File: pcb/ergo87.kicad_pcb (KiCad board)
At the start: 2 copper layers, 322.7 x 132.7 mm, 175 parts, among them U1 ItsyBitsy

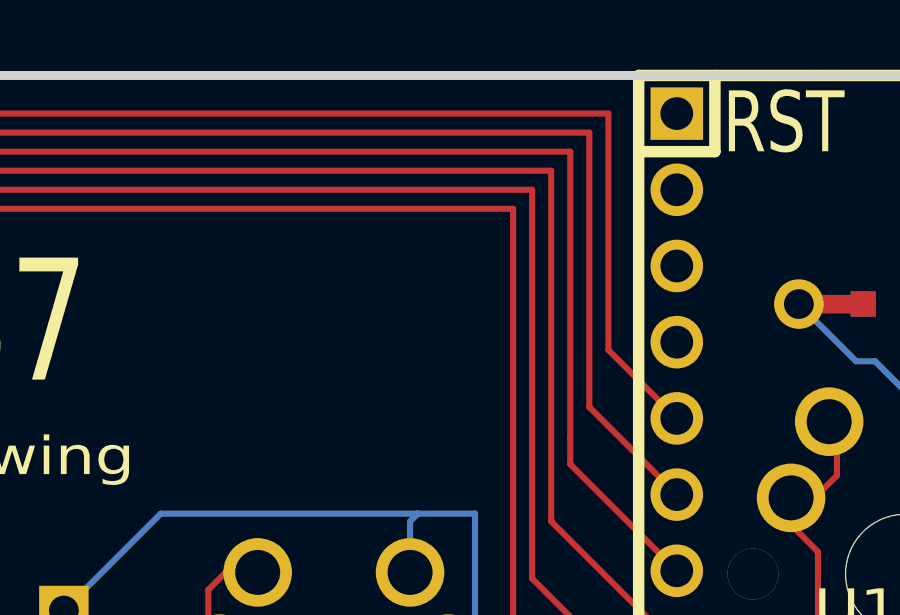
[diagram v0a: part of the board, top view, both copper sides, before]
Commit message: Add reset button footprint
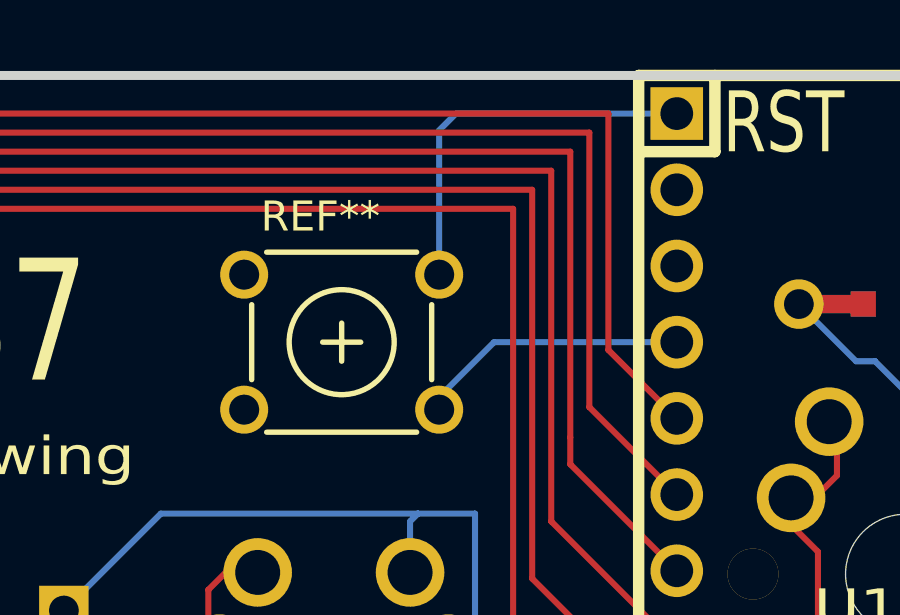
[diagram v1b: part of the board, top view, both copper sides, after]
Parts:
- added REF**: VAL**, B3F-10XX, F.Cu at (156.2, 26.7)
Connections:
- U1 pad 1: (no net) -> N-RST
- U1 pad 4: (no net) -> N-GND
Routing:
- net N-RST: track 0.00 -> 13.0 mm
- net N-GND: track 0.00 -> 9.10 mm
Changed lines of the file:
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@@
 (kicad_pcb (version 4) (host pcbnew 4.0.7)
   (general
-    (links 435)
+    (links 437)
     (no_connects 0)
     (area 13.498331 17.335499 336.501679 150.650001)
     (thickness 1.6002)
     (drawings 11)
-    (tracks 1890)
+    (tracks 1896)
     (zones 0)
-    (modules 175)
-    (nets 109)
+    (modules 176)
+    (nets 111)
   )
   (page User 370.002 189.992)
@@
   (net 107 N-diode-5-13)
   (net 108 N-diode-5-14)
+  (net 109 N-RST)
+  (net 110 N-GND)
   (net_class Default "This is the default net class."
     (clearance 0.254)
@@
     (uvia_dia 0.508)
     (uvia_drill 0.127)
+    (add_net N-GND)
+    (add_net N-RST)
     (add_net N-col-0)
     (add_net N-col-1)
@@
     (fp_line (start -17.78 6.35) (end -15.24 6.35) (layer F.SilkS) (width 0.381))
     (fp_line (start -15.24 6.35) (end -15.24 8.89) (layer F.SilkS) (width 0.381))
-    (pad 1 thru_hole rect (at -16.51 7.62) (size 1.7526 1.7526) (drill 1.0922) (layers *.Cu *.SilkS *.Mask))
+    (pad 1 thru_hole rect (at -16.51 7.62) (size 1.7526 1.7526) (drill 1.0922) (layers *.Cu *.SilkS *.Mask)
+      (net 109 N-RST))
     (pad 2 thru_hole circle (at -13.97 7.62) (size 1.7526 1.7526) (drill 1.0922) (layers *.Cu *.SilkS *.Mask))
     (pad 3 thru_hole circle (at -11.43 7.62) (size 1.7526 1.7526) (drill 1.0922) (layers *.Cu *.SilkS *.Mask))
-    (pad 4 thru_hole circle (at -8.89 7.62) (size 1.7526 1.7526) (drill 1.0922) (layers *.Cu *.SilkS *.Mask))
+    (pad 4 thru_hole circle (at -8.89 7.62) (size 1.7526 1.7526) (drill 1.0922) (layers *.Cu *.SilkS *.Mask)
+      (net 110 N-GND))
     (pad 5 thru_hole circle (at -6.35 7.62) (size 1.7526 1.7526) (drill 1.0922) (layers *.Cu *.SilkS *.Mask)
       (net 7 N-col-0))
@@
     (pad 99 smd rect (at 1.6637 0 10) (size 0.8382 0.8382) (layers Back B.Paste B.Mask))
   )
+  (module B3F-10XX (layer Front)
+    (at 156.21 26.67)
+    (descr "Tactile switch - SPST - 6mm")
+    (tags "tactile switch")
+    (fp_text reference REF** (at -2.7 -3.6) (layer F.SilkS)
+      (effects (font (size 1 1) (thickness 0.18)) (justify left bottom))
+    )
+    (fp_text value VAL** (at 0 4.3) (layer F.SilkS) hide
+      (effects (font (size 1 1) (thickness 0.15)))
+    )
+    (fp_line (start -3.5 -3.5) (end 3.5 -3.5) (layer F.CrtYd) (width 0.05))
+    (fp_line (start 3.5 -3.5) (end 3.5 3.5) (layer F.CrtYd) (width 0.05))
+    (fp_line (start 3.5 3.5) (end -3.5 3.5) (layer F.CrtYd) (width 0.05))
+    (fp_line (start -3.5 3.5) (end -3.5 -3.5) (layer F.CrtYd) (width 0.05))
+    (fp_line (start -3 1.25) (end -3 -1.25) (layer F.SilkS) (width 0.18))
+    (fp_line (start -2.5 3) (end 2.5 3) (layer F.SilkS) (width 0.18))
+    (fp_line (start -2.5 -3) (end 2.5 -3) (layer F.SilkS) (width 0.18))
+    (fp_line (start 3 1.25) (end 3 -1.25) (layer F.SilkS) (width 0.18))
+    (fp_circle (center 0 0) (end 1.75 0) (layer F.SilkS) (width 0.18))
+    (fp_line (start -0.635 0) (end 0.635 0) (layer F.SilkS) (width 0.18))
+    (fp_line (start 0 -0.635) (end 0 0.635) (layer F.SilkS) (width 0.18))
+    (pad 1 thru_hole circle (at -3.25 2.25) (size 1.6 1.6) (drill 1) (layers *.Cu *.Mask))
+    (pad 1 thru_hole circle (at 3.25 2.25) (size 1.6 1.6) (drill 1) (layers *.Cu *.Mask)
+      (net 110 N-GND))
+    (pad 2 thru_hole circle (at 3.25 -2.25) (size 1.6 1.6) (drill 1) (layers *.Cu *.Mask)
+      (net 109 N-RST))
+    (pad 2 thru_hole circle (at -3.25 -2.25) (size 1.6 1.6) (drill 1) (layers *.Cu *.Mask))
+  )
   (gr_text "By: Paul Ewing" (at 141.605 30.48) (layer F.SilkS)
     (effects (font (size 1.27 1.524) (thickness 0.3048)))
@@
   (segment (start 318.3243 115.687382) (end 318.3243 114.7457) (width 0.2032) (layer Back) (net 108))
   (segment (start 318.3243 114.7457) (end 320.675 112.395) (width 0.2032) (layer Back) (net 108))
+  (segment (start 159.46 24.42) (end 159.46 19.61) (width 0.2032) (layer Back) (net 109) (status 400000))
+  (segment (start 160.02 19.05) (end 167.38 19.05) (width 0.2032) (layer Back) (net 109) (status 800000))
+  (segment (start 159.46 19.61) (end 160.02 19.05) (width 0.2032) (layer Back) (net 109))
+  (segment (start 159.46 28.92) (end 159.46 28.5) (width 0.2032) (layer Back) (net 110) (status C00000))
+  (segment (start 159.46 28.5) (end 161.29 26.67) (width 0.2032) (layer Back) (net 110) (status 400000))
+  (segment (start 161.29 26.67) (end 167.38 26.67) (width 0.2032) (layer Back) (net 110) (status 800000))
 )

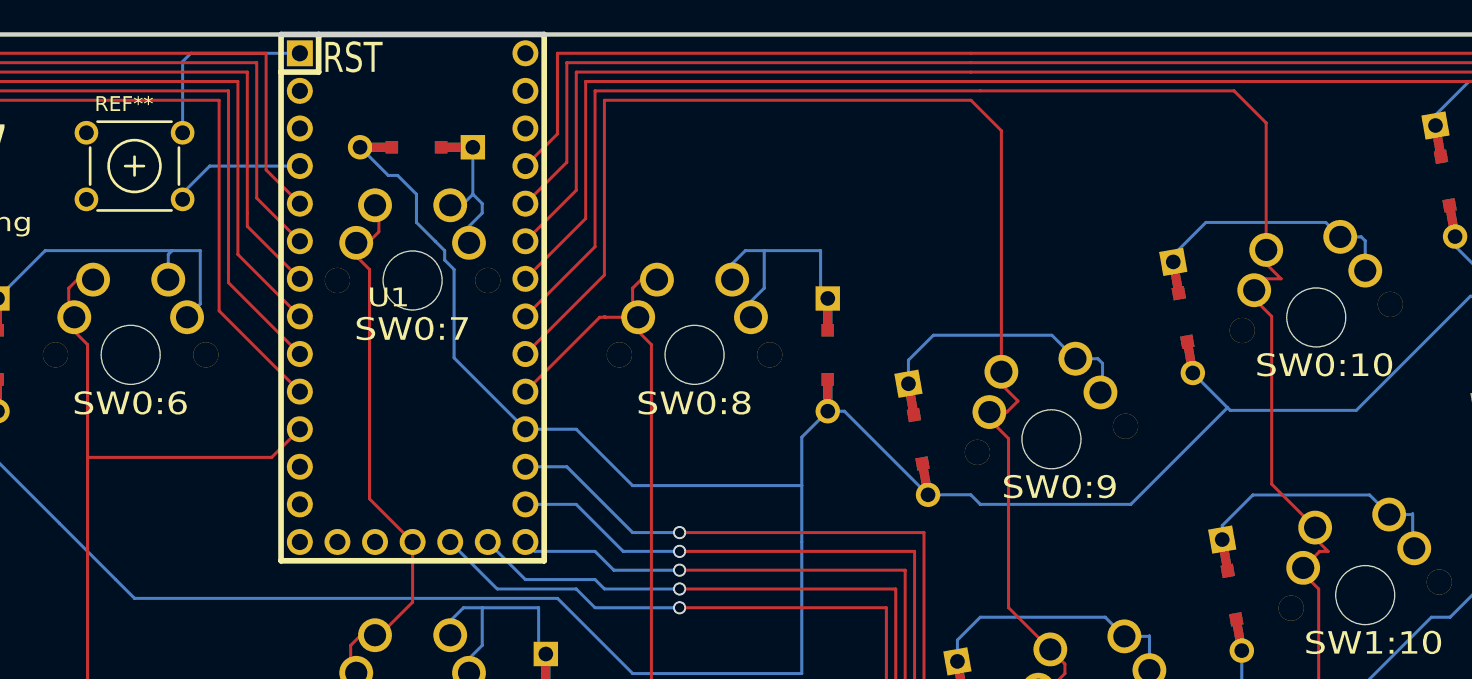
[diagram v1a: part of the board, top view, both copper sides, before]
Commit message: Start working on RGB underglow support
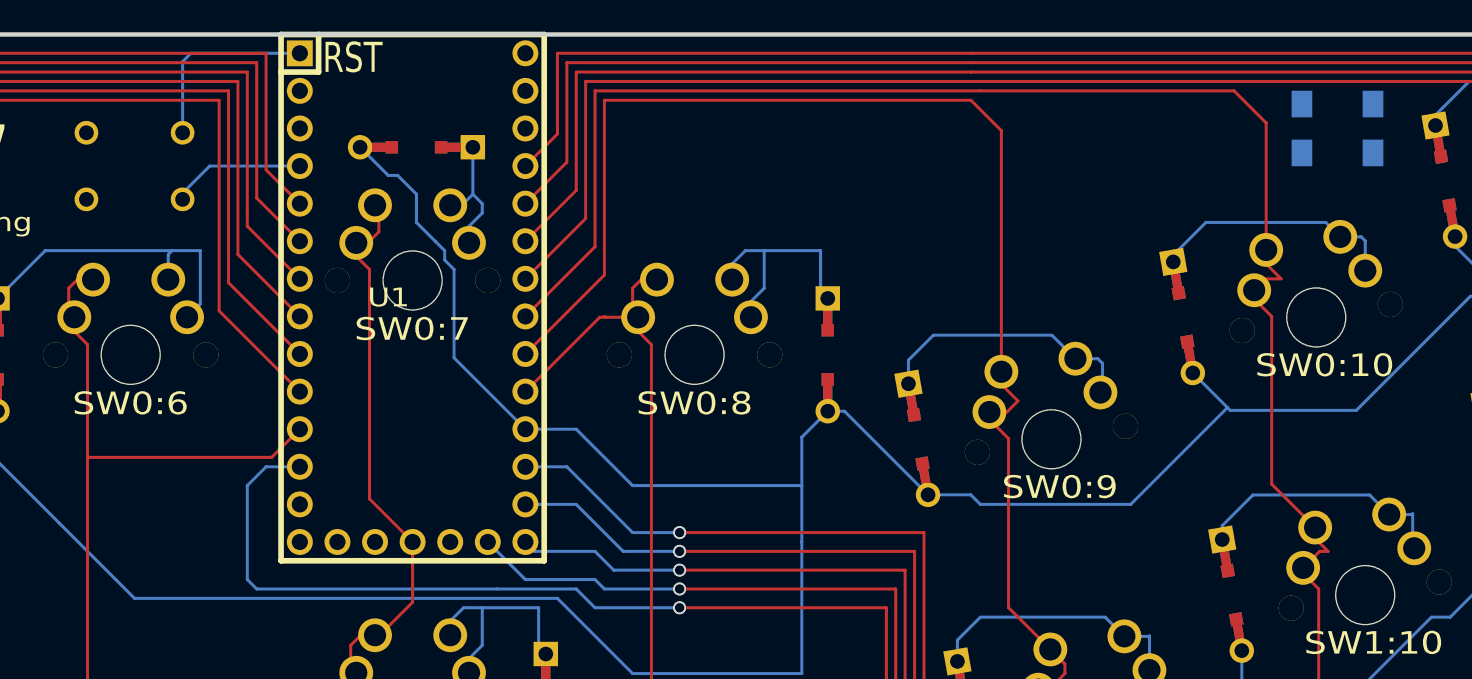
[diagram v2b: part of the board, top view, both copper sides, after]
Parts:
- removed REF**: VAL**, B3F-10XX
- added B1: VAL**, B3F-10XX, B.Cu at (156.2, 26.7)
- added LED?: VAL**, WS2812B, B.Cu at (237.5, 24.1)
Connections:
- U1 pad 12: (no net) -> N-row-5
- U1 pad 17: N-col-7 -> (no net)
- U1 pad 18: N-row-5 -> (no net)
- U1 pad 4: N-GND -> N-GND-0
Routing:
- net N-row-5: track 484.9 -> 507.6 mm
- net N-GND-0: track 0.00 -> 9.10 mm
- net N-GND: track 9.10 -> 0.00 mm

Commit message: Finish the rev2 features
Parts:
- removed LED?: VAL**, WS2812B
- added RGB0: VAL**, WS2812B, B.Cu at (236.9, 22.2)
- added RGB1: VAL**, WS2812B, B.Cu at (318.8, 50.8)
- added RGB10: VAL**, WS2812B, B.Cu at (31.2, 50.8)
- added RGB11: VAL**, WS2812B, B.Cu at (113.1, 22.2)
- added RGB2: VAL**, WS2812B, B.Cu at (328.9, 106.7)
- added RGB3: VAL**, WS2812B, B.Cu at (293.4, 130.2)
- added RGB4: VAL**, WS2812B, B.Cu at (250.8, 139.1)
- added RGB5: VAL**, WS2812B, B.Cu at (197.5, 146.1)
- added RGB6: VAL**, WS2812B, B.Cu at (152.5, 146.1)
- added RGB7: VAL**, WS2812B, B.Cu at (99.2, 139.1)
- added RGB8: VAL**, WS2812B, B.Cu at (56.6, 130.2)
- added RGB9: VAL**, WS2812B, B.Cu at (21.1, 106.7)
- moved B1 73.8 mm to (175.0, 98.0)
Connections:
- U1 pad 17: (no net) -> N-col-7
- U1 pad 18: (no net) -> N-RGB-D0
- U1 pad 2: (no net) -> N-5V-0
- U1 pad 32: (no net) -> N-GND-1
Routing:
- net N-GND-1: track 0.00 -> 931.7 mm, vias 0 -> 14
- net N-5V-0: track 0.00 -> 888.3 mm, vias 0 -> 14
- net N-RGB-D1: track 0.00 -> 107.9 mm, vias 0 -> 2
- net N-RGB-D11: track 0.00 -> 103.6 mm, vias 0 -> 2
- net N-RST: track 13.0 -> 100.6 mm, vias 0 -> 3
- net N-RGB-D0: track 0.00 -> 84.6 mm, vias 0 -> 1
- net N-GND-0: track 9.10 -> 91.4 mm, vias 0 -> 3
- net N-row-5: track 507.6 -> 579.2 mm
- net N-RGB-D10: track 0.00 -> 65.3 mm
- net N-RGB-D2: track 0.00 -> 60.1 mm
- net N-RGB-D7: track 0.00 -> 56.3 mm
- net N-RGB-D3: track 0.00 -> 55.9 mm
- net N-RGB-D5: track 0.00 -> 53.9 mm
- net N-RGB-D9: track 0.00 -> 48.2 mm
- net N-RGB-D4: track 0.00 -> 41.9 mm
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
